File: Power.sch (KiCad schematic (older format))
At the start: 13 parts

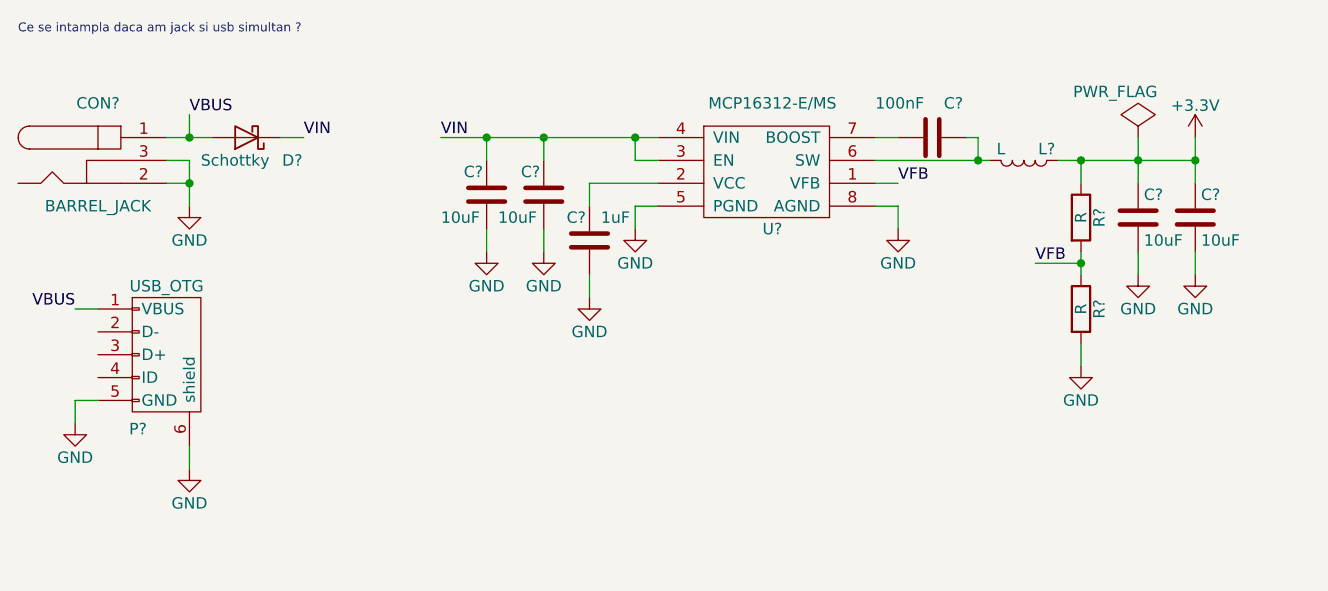
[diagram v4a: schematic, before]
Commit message: Finished interfaces.
Finished MAX3232 serial to RS232 interface.
Finished ST3485 serial to RS485 interface.
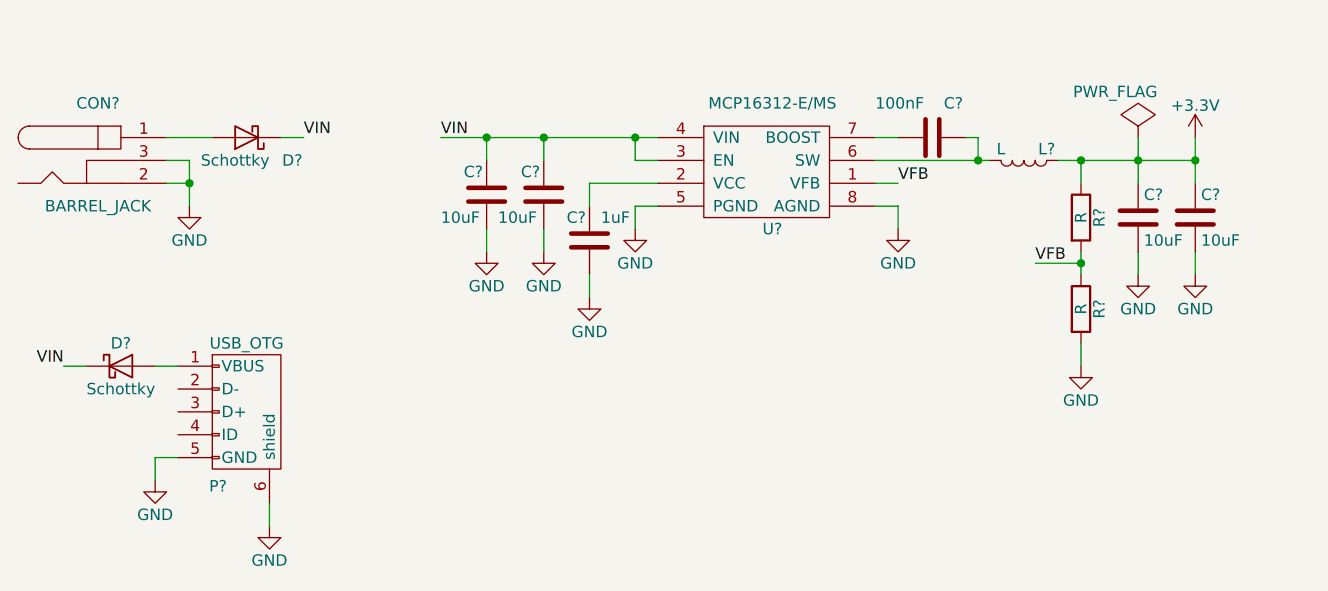
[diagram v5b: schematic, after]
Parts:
- added D?: Schottky, symbol D_Schottky
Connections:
- net VIN: now also D?.1 (K)
- net VBUS: no longer names the net of CON?.1, D?.2 (A)
- net VBUS: no longer P?.1 (VBUS)
- new net: D?.2 (A), P?.1 (VBUS)
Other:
- note removed: "Ce se intampla daca am jack si usb simultan ?"
- moved on the sheet: P?
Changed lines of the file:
@@
 LIBS:MCP2200
 LIBS:w_connectors
+LIBS:max-lin
 LIBS:E-GIF-M-Board-cache
 EELAYER 25 0
@@
 $Descr A4 11693 8268
 encoding utf-8
-Sheet 2 5
+Sheet 2 7
 Title ""
 Date ""
@@
 L USB_OTG P?
 U 1 1 587BE3DA
-P 3900 3450
-F 0 "P?" V 4225 3325 50  0000 C CNN
-F 1 "USB_OTG" V 3600 3450 50  0000 C CNN
-F 2 "" V 3850 3350 50  0000 C CNN
-F 3 "" V 3850 3350 50  0000 C CNN
-	1    3900 3450
+P 4250 3700
+F 0 "P?" V 4575 3575 50  0000 C CNN
+F 1 "USB_OTG" V 3950 3700 50  0000 C CNN
+F 2 "" V 4200 3600 50  0000 C CNN
+F 3 "" V 4200 3600 50  0000 C CNN
+	1    4250 3700
 	0    1    1    0
 $EndComp
 $Comp
-L GND #PWR?
+L GND #PWR01
 U 1 1 587BE675
 P 4000 2800
-F 0 "#PWR?" H 4000 2550 50  0001 C CNN
+F 0 "#PWR01" H 4000 2550 50  0001 C CNN
 F 1 "GND" H 4000 2650 50  0000 C CNN
 F 2 "" H 4000 2800 50  0000 C CNN
@@
 $EndComp
 $Comp
-L GND #PWR?
+L GND #PWR02
 U 1 1 587BE697
-P 4000 3950
-F 0 "#PWR?" H 4000 3700 50  0001 C CNN
-F 1 "GND" H 4000 3800 50  0000 C CNN
-F 2 "" H 4000 3950 50  0000 C CNN
-F 3 "" H 4000 3950 50  0000 C CNN
-	1    4000 3950
-	1    0    0    -1
-$EndComp
-$Comp
-L GND #PWR?
+P 4350 4200
+F 0 "#PWR02" H 4350 3950 50  0001 C CNN
+F 1 "GND" H 4350 4050 50  0000 C CNN
+F 2 "" H 4350 4200 50  0000 C CNN
+F 3 "" H 4350 4200 50  0000 C CNN
+	1    4350 4200
+	1    0    0    -1
+$EndComp
+$Comp
+L GND #PWR03
 U 1 1 587BE6AA
-P 3500 3750
-F 0 "#PWR?" H 3500 3500 50  0001 C CNN
-F 1 "GND" H 3500 3600 50  0000 C CNN
-F 2 "" H 3500 3750 50  0000 C CNN
-F 3 "" H 3500 3750 50  0000 C CNN
-	1    3500 3750
-	1    0    0    -1
-$EndComp
-Text Label 3500 3250 2    50   ~ 0
-VBUS
-$Comp
-L PWR_FLAG #FLG?
+P 3850 4000
+F 0 "#PWR03" H 3850 3750 50  0001 C CNN
+F 1 "GND" H 3850 3850 50  0000 C CNN
+F 2 "" H 3850 4000 50  0000 C CNN
+F 3 "" H 3850 4000 50  0000 C CNN
+	1    3850 4000
+	1    0    0    -1
+$EndComp
+$Comp
+L PWR_FLAG #FLG04
 U 1 1 587BE76C
 P 8150 2500
-F 0 "#FLG?" H 8150 2595 50  0001 C CNN
+F 0 "#FLG04" H 8150 2595 50  0001 C CNN
 F 1 "PWR_FLAG" H 8050 2700 50  0000 C CNN
 F 2 "" H 8150 2500 50  0000 C CNN
@@
 	1    0    0    -1
 $EndComp
-Text Label 4000 2400 0    50   ~ 0
-VBUS
 $Comp
 L D_Schottky D?
@@
 	-1   0    0    1
 $EndComp
-Text Notes 3250 2050 0    39   ~ 0
-Ce se intampla daca am jack si usb simultan ?
 $Comp
 L MCP16312-E/MS U?
@@
 $EndComp
 $Comp
-L GND #PWR?
+L GND #PWR05
 U 1 1 587BECE9
 P 5950 2900
-F 0 "#PWR?" H 5950 2650 50  0001 C CNN
+F 0 "#PWR05" H 5950 2650 50  0001 C CNN
 F 1 "GND" H 5950 2750 50  0000 C CNN
 F 2 "" H 5950 2900 50  0000 C CNN
@@
 $EndComp
 $Comp
-L GND #PWR?
+L GND #PWR06
 U 1 1 587BED67
 P 5750 3200
-F 0 "#PWR?" H 5750 2950 50  0001 C CNN
+F 0 "#PWR06" H 5750 2950 50  0001 C CNN
 F 1 "GND" H 5750 3050 50  0000 C CNN
 F 2 "" H 5750 3200 50  0000 C CNN
@@
 $EndComp
 $Comp
-L GND #PWR?
+L GND #PWR07
 U 1 1 587BEE32
 P 5550 3000
-F 0 "#PWR?" H 5550 2750 50  0001 C CNN
+F 0 "#PWR07" H 5550 2750 50  0001 C CNN
 F 1 "GND" H 5550 2850 50  0000 C CNN
 F 2 "" H 5550 3000 50  0000 C CNN
@@
 $EndComp
 $Comp
-L GND #PWR?
+L GND #PWR08
 U 1 1 587BEE52
 P 5300 3000
-F 0 "#PWR?" H 5300 2750 50  0001 C CNN
+F 0 "#PWR08" H 5300 2750 50  0001 C CNN
 F 1 "GND" H 5300 2850 50  0000 C CNN
 F 2 "" H 5300 3000 50  0000 C CNN
@@
 VIN
 $Comp
-L GND #PWR?
+L GND #PWR09
 U 1 1 587BF3B1
 P 7100 2900
-F 0 "#PWR?" H 7100 2650 50  0001 C CNN
+F 0 "#PWR09" H 7100 2650 50  0001 C CNN
 F 1 "GND" H 7100 2750 50  0000 C CNN
 F 2 "" H 7100 2900 50  0000 C CNN
@@
 $EndComp
 $Comp
-L GND #PWR?
+L GND #PWR010
 U 1 1 587BF576
 P 7900 3500
-F 0 "#PWR?" H 7900 3250 50  0001 C CNN
+F 0 "#PWR010" H 7900 3250 50  0001 C CNN
 F 1 "GND" H 7900 3350 50  0000 C CNN
 F 2 "" H 7900 3500 50  0000 C CNN
@@
 $EndComp
 $Comp
-L GND #PWR?
+L GND #PWR011
 U 1 1 587BFB09
 P 8150 3100
-F 0 "#PWR?" H 8150 2850 50  0001 C CNN
+F 0 "#PWR011" H 8150 2850 50  0001 C CNN
 F 1 "GND" H 8150 2950 50  0000 C CNN
 F 2 "" H 8150 3100 50  0000 C CNN
@@
 $EndComp
 $Comp
-L GND #PWR?
+L GND #PWR012
 U 1 1 587BFB3B
 P 8400 3100
-F 0 "#PWR?" H 8400 2850 50  0001 C CNN
+F 0 "#PWR012" H 8400 2850 50  0001 C CNN
 F 1 "GND" H 8400 2950 50  0000 C CNN
 F 2 "" H 8400 3100 50  0000 C CNN
@@
 $EndComp
 $Comp
-L +3.3V #PWR?
+L +3.3V #PWR013
 U 1 1 587C072D
 P 8400 2500
-F 0 "#PWR?" H 8400 2350 50  0001 C CNN
+F 0 "#PWR013" H 8400 2350 50  0001 C CNN
 F 1 "+3.3V" H 8400 2640 50  0000 C CNN
 F 2 "" H 8400 2500 50  0000 C CNN
@@
 $EndComp
 Wire Wire Line
-	3600 3250 3500 3250
-Wire Wire Line
-	3500 3650 3500 3750
-Wire Wire Line
-	3500 3650 3600 3650
-Wire Wire Line
-	4000 3950 4000 3850
+	3950 3500 3850 3500
+Wire Wire Line
+	3850 3900 3850 4000
+Wire Wire Line
+	3850 3900 3950 3900
+Wire Wire Line
+	4350 4200 4350 4100
 Wire Wire Line
 	4000 2600 4000 2800
@@
 	3900 2500 4100 2500
 Wire Wire Line
-	4000 2500 4000 2400
-Connection ~ 4000 2500
-Wire Wire Line
 	4500 2500 4400 2500
 Wire Wire Line
@@
 	7100 2500 7000 2500
 Connection ~ 8400 2600
+$Comp
+L D_Schottky D?
+U 1 1 58917724
+P 3700 3500
+F 0 "D?" H 3700 3600 50  0000 C CNN
+F 1 "Schottky" H 3700 3400 50  0000 C CNN
+F 2 "" H 3700 3500 50  0000 C CNN
+F 3 "" H 3700 3500 50  0000 C CNN
+	1    3700 3500
+	1    0    0    -1
+$EndComp
+Text Label 3450 3500 2    50   ~ 0
+VIN
+Wire Wire Line
+	3450 3500 3550 3500
 $EndSCHEMATC

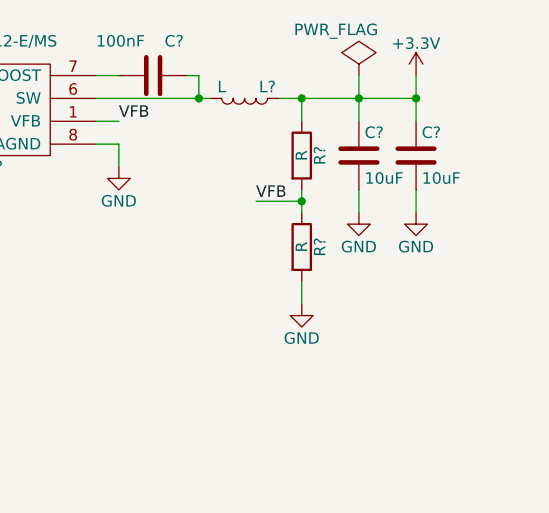
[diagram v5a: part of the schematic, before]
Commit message: Added to scheamtic.
Added reset circuit for Aiya, power led for 3V3 line, USB type A connectors for USBB and USBC.
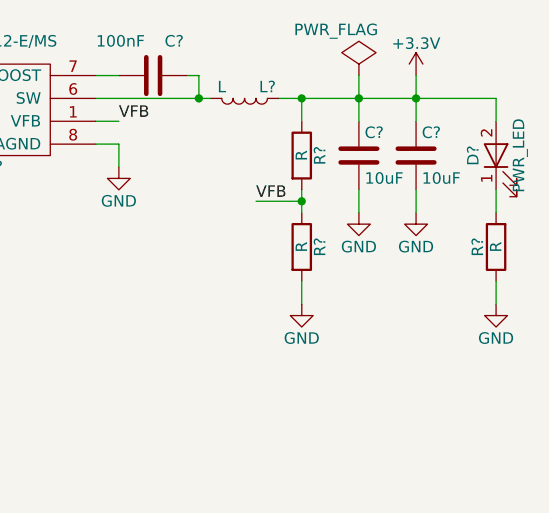
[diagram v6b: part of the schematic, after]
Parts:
- added D?: PWR_LED, symbol LED
- added R?: R, symbol R
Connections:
- net +3V3: now also D?.2 (A)
- net GND: now also R?.1
- new net: D?.1 (K), R?.2
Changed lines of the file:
@@
 LIBS:w_connectors
 LIBS:max-lin
+LIBS:IHE
 LIBS:E-GIF-M-Board-cache
 EELAYER 25 0
@@
 	7900 2700 7900 2600
 Wire Wire Line
-	7800 2600 8400 2600
+	7800 2600 8750 2600
 Wire Wire Line
 	8150 2500 8150 2700
@@
 Wire Wire Line
 	3450 3500 3550 3500
+$Comp
+L LED D?
+U 1 1 589814D5
+P 8750 2850
+F 0 "D?" H 8750 2950 50  0000 C CNN
+F 1 "PWR_LED" H 8750 2750 50  0000 C CNN
+F 2 "" H 8750 2850 50  0000 C CNN
+F 3 "" H 8750 2850 50  0000 C CNN
+	1    8750 2850
+	0    -1   -1   0
+$EndComp
+$Comp
+L R R?
+U 1 1 58981539
+P 8750 3250
+F 0 "R?" V 8830 3250 50  0000 C CNN
+F 1 "R" V 8750 3250 50  0000 C CNN
+F 2 "" V 8680 3250 50  0000 C CNN
+F 3 "" H 8750 3250 50  0000 C CNN
+	1    8750 3250
+	-1   0    0    1
+$EndComp
+$Comp
+L GND #PWR?
+U 1 1 58981582
+P 8750 3500
+F 0 "#PWR?" H 8750 3250 50  0001 C CNN
+F 1 "GND" H 8750 3350 50  0000 C CNN
+F 2 "" H 8750 3500 50  0000 C CNN
+F 3 "" H 8750 3500 50  0000 C CNN
+	1    8750 3500
+	1    0    0    -1
+$EndComp
+Wire Wire Line
+	8750 3400 8750 3500
+Wire Wire Line
+	8750 3000 8750 3100
+Wire Wire Line
+	8750 2600 8750 2700
 $EndSCHEMATC

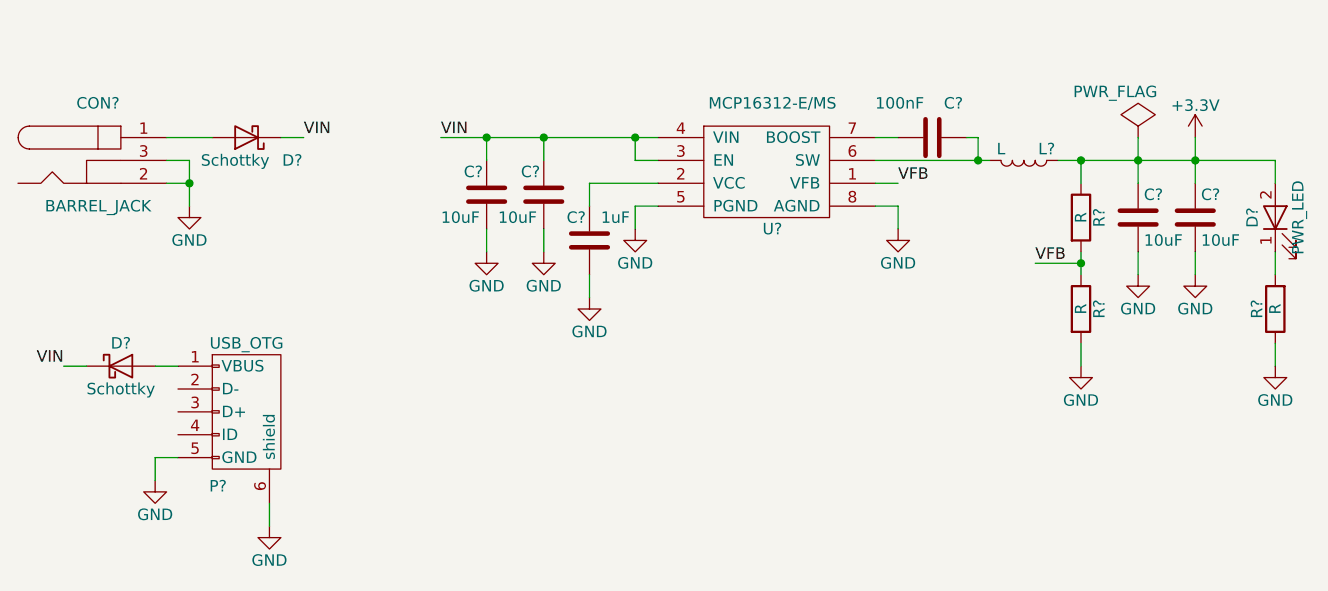
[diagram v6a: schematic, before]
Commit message: Schematic correction
Corrected the direction on some signals. Added a pin header for general development.
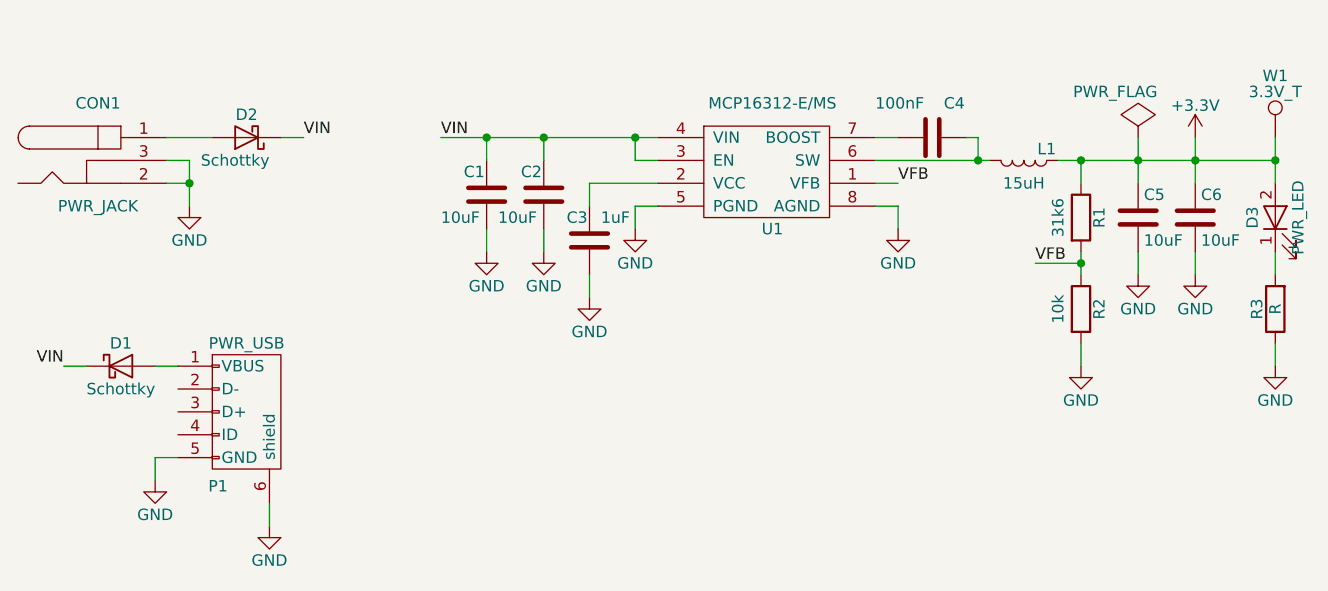
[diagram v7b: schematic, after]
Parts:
- added W1: 3.3V_T, symbol TEST_1P
- C1, C2, C3, C4, C5, C6: renamed from C?; footprint (none) -> Capacitors_SMD:C_0603_HandSoldering
- CON1: renamed from CON?; value BARREL_JACK -> PWR_JACK
- L1: renamed from L?; value L -> 15uH
- P1: renamed from P?; value USB_OTG -> PWR_USB
- R1: renamed from R?; value R -> 31k6; footprint (none) -> Resistors_SMD:R_0603_HandSoldering
- R2: renamed from R?; value R -> 10k; footprint (none) -> Resistors_SMD:R_0603_HandSoldering
- R3: renamed from R?; footprint (none) -> Resistors_SMD:R_0603_HandSoldering
- gave numbers to parts that had none: 4
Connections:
- net +3V3: now also W1.1
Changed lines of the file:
@@
 $EndDescr
 $Comp
-L BARREL_JACK CON?
+L BARREL_JACK CON1
 U 1 1 587BDB9B
 P 3600 2600
-F 0 "CON?" H 3600 2850 50  0000 C CNN
-F 1 "BARREL_JACK" H 3600 2400 50  0000 C CNN
-F 2 "" H 3600 2600 50  0000 C CNN
+F 0 "CON1" H 3600 2850 50  0000 C CNN
+F 1 "PWR_JACK" H 3600 2400 50  0000 C CNN
+F 2 "" H 3600 2600 50  0001 C CNN
 F 3 "" H 3600 2600 50  0000 C CNN
 	1    3600 2600
@@
 $EndComp
 $Comp
-L USB_OTG P?
+L USB_OTG P1
 U 1 1 587BE3DA
 P 4250 3700
-F 0 "P?" V 4575 3575 50  0000 C CNN
-F 1 "USB_OTG" V 3950 3700 50  0000 C CNN
-F 2 "" V 4200 3600 50  0000 C CNN
+F 0 "P1" V 4575 3575 50  0000 C CNN
+F 1 "PWR_USB" V 3950 3700 50  0000 C CNN
+F 2 "" V 4200 3600 50  0001 C CNN
 F 3 "" V 4200 3600 50  0000 C CNN
 	1    4250 3700
@@
 $EndComp
 $Comp
-L D_Schottky D?
+L D_Schottky D2
 U 1 1 587BE7B1
 P 4250 2500
-F 0 "D?" H 4050 2600 50  0000 C CNN
+F 0 "D2" H 4250 2400 50  0000 C CNN
 F 1 "Schottky" H 4300 2600 50  0000 C CNN
-F 2 "" H 4250 2500 50  0000 C CNN
+F 2 "" H 4250 2500 50  0001 C CNN
 F 3 "" H 4250 2500 50  0000 C CNN
 	1    4250 2500
@@
 $EndComp
 $Comp
-L MCP16312-E/MS U?
+L MCP16312-E/MS U1
 U 1 1 587BE8EA
 P 6500 2650
-F 0 "U?" H 6550 2400 50  0000 C CNN
+F 0 "U1" H 6550 2400 50  0000 C CNN
 F 1 "MCP16312-E/MS" H 6550 2950 50  0000 C CNN
 F 2 "" H 6600 2900 60  0001 C CNN
@@
 VIN
 $Comp
-L C C?
+L C C3
 U 1 1 587BEC23
 P 5750 2950
-F 0 "C?" H 5650 3050 50  0000 L CNN
+F 0 "C3" H 5650 3050 50  0000 L CNN
 F 1 "1uF" H 5800 3050 50  0000 L CNN
-F 2 "" H 5788 2800 50  0000 C CNN
+F 2 "Capacitors_SMD:C_0603_HandSoldering" H 5788 2800 50  0001 C CNN
 F 3 "" H 5750 2950 50  0000 C CNN
 	1    5750 2950
@@
 $EndComp
 $Comp
-L C C?
+L C C1
 U 1 1 587BEC9F
 P 5300 2750
-F 0 "C?" H 5200 2850 50  0000 L CNN
+F 0 "C1" H 5200 2850 50  0000 L CNN
 F 1 "10uF" H 5100 2650 50  0000 L CNN
-F 2 "" H 5338 2600 50  0000 C CNN
+F 2 "Capacitors_SMD:C_0603_HandSoldering" H 5338 2600 50  0001 C CNN
 F 3 "" H 5300 2750 50  0000 C CNN
 	1    5300 2750
@@
 $EndComp
 $Comp
-L C C?
+L C C2
 U 1 1 587BEDBB
 P 5550 2750
-F 0 "C?" H 5450 2850 50  0000 L CNN
+F 0 "C2" H 5450 2850 50  0000 L CNN
 F 1 "10uF" H 5350 2650 50  0000 L CNN
-F 2 "" H 5588 2600 50  0000 C CNN
+F 2 "Capacitors_SMD:C_0603_HandSoldering" H 5588 2600 50  0001 C CNN
 F 3 "" H 5550 2750 50  0000 C CNN
 	1    5550 2750
@@
 $EndComp
 $Comp
-L L L?
+L L L1
 U 1 1 587BF430
 P 7650 2600
-F 0 "L?" V 7600 2700 50  0000 C CNN
-F 1 "L" V 7600 2500 50  0000 C CNN
-F 2 "" H 7650 2600 50  0000 C CNN
+F 0 "L1" V 7600 2700 50  0000 C CNN
+F 1 "15uH" V 7750 2600 50  0000 C CNN
+F 2 "" H 7650 2600 50  0001 C CNN
 F 3 "" H 7650 2600 50  0000 C CNN
 	1    7650 2600
@@
 $EndComp
 $Comp
-L R R?
+L R R1
 U 1 1 587BF4C5
 P 7900 2850
-F 0 "R?" V 7980 2850 50  0000 C CNN
-F 1 "R" V 7900 2850 50  0000 C CNN
-F 2 "" V 7830 2850 50  0000 C CNN
+F 0 "R1" V 7980 2850 50  0000 C CNN
+F 1 "31k6" V 7800 2850 50  0000 C CNN
+F 2 "Resistors_SMD:R_0603_HandSoldering" V 7830 2850 50  0001 C CNN
 F 3 "" H 7900 2850 50  0000 C CNN
 	1    7900 2850
@@
 $EndComp
 $Comp
-L R R?
+L R R2
 U 1 1 587BF53A
 P 7900 3250
-F 0 "R?" V 7980 3250 50  0000 C CNN
-F 1 "R" V 7900 3250 50  0000 C CNN
-F 2 "" V 7830 3250 50  0000 C CNN
+F 0 "R2" V 7980 3250 50  0000 C CNN
+F 1 "10k" V 7800 3250 50  0000 C CNN
+F 2 "Resistors_SMD:R_0603_HandSoldering" V 7830 3250 50  0001 C CNN
 F 3 "" H 7900 3250 50  0000 C CNN
 	1    7900 3250
@@
 VFB
 $Comp
-L C C?
+L C C4
 U 1 1 587BF8DF
 P 7250 2500
-F 0 "C?" V 7100 2550 50  0000 L CNN
+F 0 "C4" V 7100 2550 50  0000 L CNN
 F 1 "100nF" V 7100 2250 50  0000 L CNN
-F 2 "" H 7288 2350 50  0000 C CNN
+F 2 "Capacitors_SMD:C_0603_HandSoldering" H 7288 2350 50  0001 C CNN
 F 3 "" H 7250 2500 50  0000 C CNN
 	1    7250 2500
@@
 $EndComp
 $Comp
-L C C?
+L C C5
 U 1 1 587BF9EB
 P 8150 2850
-F 0 "C?" H 8175 2950 50  0000 L CNN
+F 0 "C5" H 8175 2950 50  0000 L CNN
 F 1 "10uF" H 8175 2750 50  0000 L CNN
-F 2 "" H 8188 2700 50  0000 C CNN
+F 2 "Capacitors_SMD:C_0603_HandSoldering" H 8188 2700 50  0001 C CNN
 F 3 "" H 8150 2850 50  0000 C CNN
 	1    8150 2850
@@
 $EndComp
 $Comp
-L C C?
+L C C6
 U 1 1 587BFA41
 P 8400 2850
-F 0 "C?" H 8425 2950 50  0000 L CNN
+F 0 "C6" H 8425 2950 50  0000 L CNN
 F 1 "10uF" H 8425 2750 50  0000 L CNN
-F 2 "" H 8438 2700 50  0000 C CNN
+F 2 "Capacitors_SMD:C_0603_HandSoldering" H 8438 2700 50  0001 C CNN
 F 3 "" H 8400 2850 50  0000 C CNN
 	1    8400 2850
@@
 Connection ~ 8400 2600
 $Comp
-L D_Schottky D?
+L D_Schottky D1
 U 1 1 58917724
 P 3700 3500
-F 0 "D?" H 3700 3600 50  0000 C CNN
+F 0 "D1" H 3700 3600 50  0000 C CNN
 F 1 "Schottky" H 3700 3400 50  0000 C CNN
-F 2 "" H 3700 3500 50  0000 C CNN
+F 2 "" H 3700 3500 50  0001 C CNN
 F 3 "" H 3700 3500 50  0000 C CNN
 	1    3700 3500
@@
 	3450 3500 3550 3500
 $Comp
-L LED D?
+L LED D3
 U 1 1 589814D5
 P 8750 2850
-F 0 "D?" H 8750 2950 50  0000 C CNN
+F 0 "D3" H 8750 2950 50  0000 C CNN
 F 1 "PWR_LED" H 8750 2750 50  0000 C CNN
-F 2 "" H 8750 2850 50  0000 C CNN
+F 2 "" H 8750 2850 50  0001 C CNN
 F 3 "" H 8750 2850 50  0000 C CNN
 	1    8750 2850
@@
 $EndComp
 $Comp
-L R R?
+L R R3
 U 1 1 58981539
 P 8750 3250
-F 0 "R?" V 8830 3250 50  0000 C CNN
+F 0 "R3" V 8830 3250 50  0000 C CNN
 F 1 "R" V 8750 3250 50  0000 C CNN
-F 2 "" V 8680 3250 50  0000 C CNN
+F 2 "Resistors_SMD:R_0603_HandSoldering" V 8680 3250 50  0001 C CNN
 F 3 "" H 8750 3250 50  0000 C CNN
 	1    8750 3250
@@
 $EndComp
 $Comp
-L GND #PWR?
+L GND #PWR014
 U 1 1 58981582
 P 8750 3500
-F 0 "#PWR?" H 8750 3250 50  0001 C CNN
+F 0 "#PWR014" H 8750 3250 50  0001 C CNN
 F 1 "GND" H 8750 3350 50  0000 C CNN
 F 2 "" H 8750 3500 50  0000 C CNN
@@
 	8750 3000 8750 3100
 Wire Wire Line
-	8750 2600 8750 2700
+	8750 2500 8750 2700
+$Comp
+L TEST_1P W1
+U 1 1 589E5880
+P 8750 2500
+F 0 "W1" H 8750 2770 50  0000 C CNN
+F 1 "3.3V_T" H 8750 2700 50  0000 C CNN
+F 2 "" H 8950 2500 50  0001 C CNN
+F 3 "" H 8950 2500 50  0000 C CNN
+	1    8750 2500
+	1    0    0    -1
+$EndComp
+Connection ~ 8750 2600
 $EndSCHEMATC
